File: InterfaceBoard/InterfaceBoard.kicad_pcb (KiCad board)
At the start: 2 copper layers, 100 x 86 mm, 184 parts, among them J1 SWD, J2 USB_B, J3 Keithley_50-Pin_Connector, J4 DB9_Female_MountingHoles, J5 SPI, J6 RS232, J7 UART, J8 I2C, P1 RB1-125BAG1A, Q1 BC848W, Q2 BC848W, Q3 BC848W, Q4 BC856W, SW1 PTS810, SW2 PTS810, U1 W5500, U2 FT231XQ, U3 MAX3232, U4 STM32G0B1RET, U5 AP62250Z6, Y1 25 MHz, Y2 32.768 kHz, Y3 24 MHz

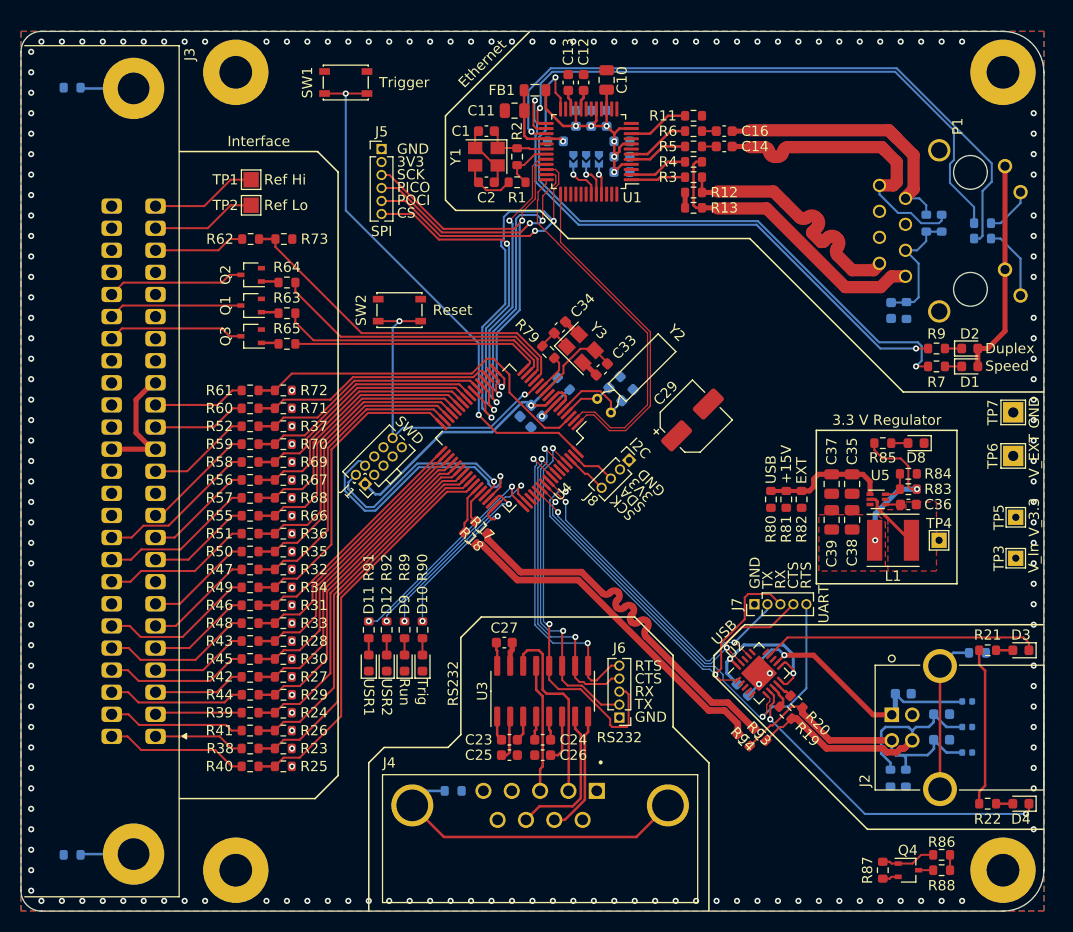
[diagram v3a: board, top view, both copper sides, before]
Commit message: InterfaceBoard: Fully route board.
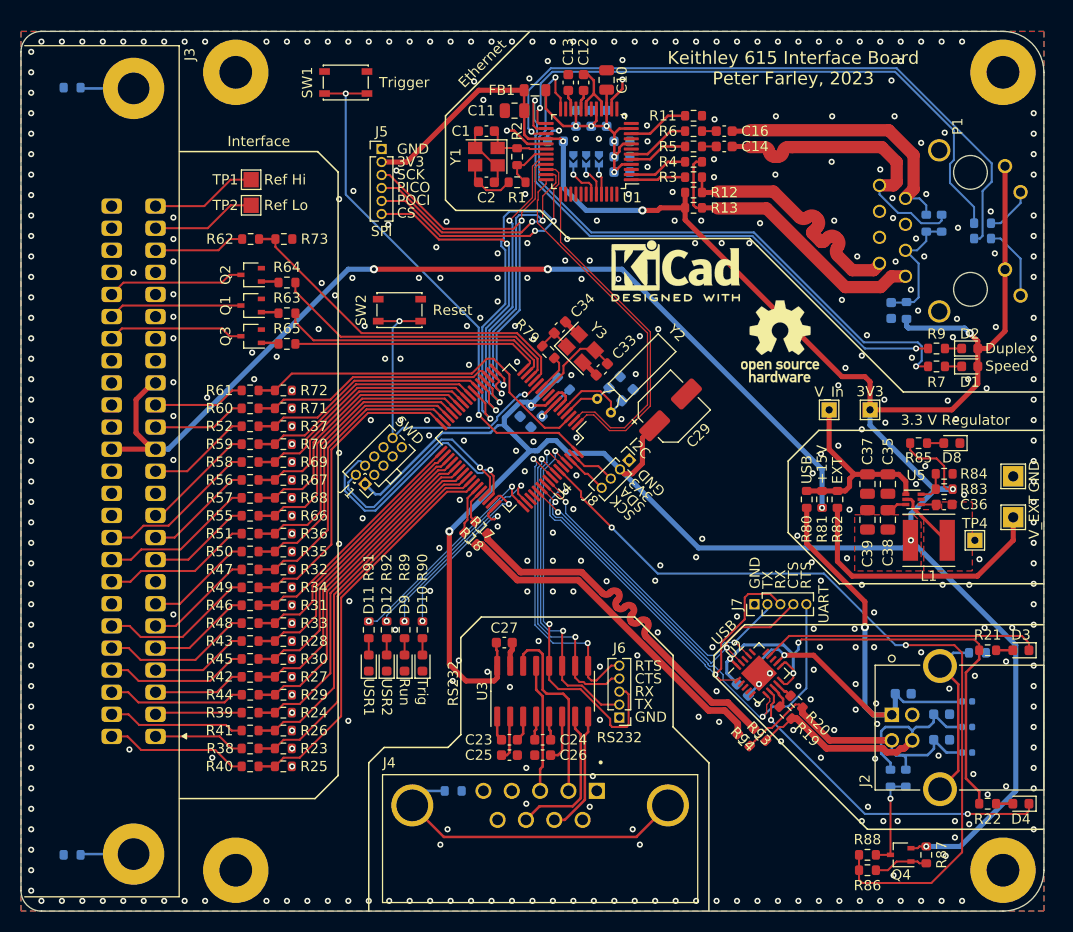
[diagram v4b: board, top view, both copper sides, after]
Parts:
- added REF**: OSHW-Logo_7.5x8mm_SilkScreen, Symbol:OSHW-Logo_7.5x8mm_SilkScreen, F.Cu at (114.2, 59.3)
- added REF**: KiCad-Logo2_5mm_SilkScreen, Symbol:KiCad-Logo2_5mm_SilkScreen, F.Cu at (104.0, 52.4)
- TP5: value V_3.3 -> 3V3
- moved TP3 23.3 mm to (119.0, 66.0), turned to 180 degrees
- moved TP5 17.7 mm to (123.0, 66.0), turned to 180 degrees
- moved R86 7.40 mm to (122.8, 111.0), turned to 0 degrees
- moved R88 7.40 mm to (122.8, 109.5), turned to 180 degrees
- moved TP7 6.25 mm to (137.0, 72.5)
- moved TP6 6.00 mm to (137.0, 76.5)
- moved R87 4.51 mm to (128.5, 109.5), turned to 90 degrees
- moved C35 3.50 mm to (124.8, 73.2)
- moved C36 3.50 mm to (130.2, 75.2)
- moved C37 3.50 mm to (122.8, 73.2)
- moved C38 3.50 mm to (124.8, 76.8)
- moved C39 3.50 mm to (122.8, 76.8)
- moved D8 3.50 mm to (131.0, 69.2)
- moved L1 3.50 mm to (128.8, 78.8)
- moved R80 3.50 mm to (116.8, 74.8)
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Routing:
- net +3V3: track 79.9 -> 300.9 mm, vias 4 -> 8
- net +15V: track 12.7 -> 97.0 mm, vias 0 -> 3
- net /MCU/USB_PULLUP: track 1.50 -> 80.4 mm, vias 0 -> 2
- net /Power Supply/V_EXT: track 0.00 -> 26.7 mm
- net /Power Supply/V_USB: track 27.8 -> 52.5 mm, vias 1 -> 2
- net /USB/FTDI_VCC: track 32.7 -> 53.2 mm, vias 2 -> 3
- net GND: track 15.5 -> 33.2 mm, vias 186 -> 415
- net Net-(R75-Pad2): track 1.43 -> 9.60 mm, vias 0 -> 1
- net /Power Supply/V_IN: track 12.2 -> 19.5 mm
- net /MCU/SWD_SWDIO: track 20.9 -> 22.5 mm
- net Net-(J2-PadSH1): track 15.4 -> 16.9 mm
- net /Ethernet Interface/ETH_PORT_RX+: track 27.5 -> 26.5 mm
- net /MCU/USB_UART_TX: track 34.6 -> 33.8 mm
- net /MCU/RS232_TX: track 33.8 -> 33.0 mm
- net /MCU/RS232_RX: track 39.6 -> 39.0 mm
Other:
- board text added: "Keithley 615 Interface Board Peter Farley, 2023"

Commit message: InterfaceBoard: Geographical reannotation.
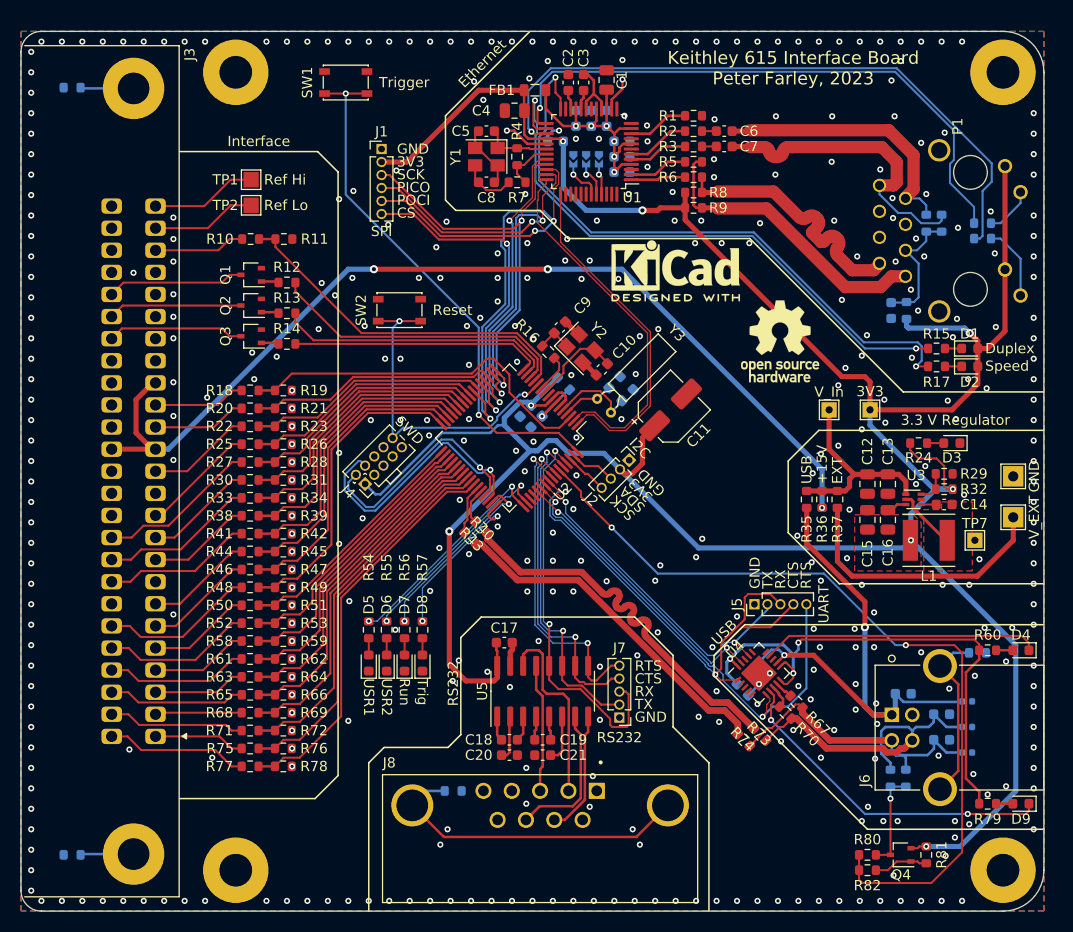
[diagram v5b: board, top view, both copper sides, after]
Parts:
- renumbered C10 to C1, C33 to C10, C29 to C11, C37 to C12, C35 to C13, C36 to C14, C39 to C15, C38 to C16, C27 to C17, C23 to C18, C24 to C19, C13 to C2, C25 to C20, C26 to C21, C6 to C22, C4 to C23, C9 to C24, C3 to C25, C8 to C26, C5 to C27, C7 to C28, C15 to C29, C12 to C3, C31 to C30, C32 to C31, C28 to C32, C30 to C33, C21 to C34, C22 to C35, C20 to C36, C19 to C37, C17 to C38, C18 to C39, C11 to C4, C1 to C5, C16 to C6, C14 to C7, C2 to C8, C34 to C9, D2 to D1, D5 to D10, D7 to D11, D6 to D12, D1 to D2, D8 to D3, D3 to D4, D11 to D5, D12 to D6, D9 to D7, D10 to D8, D4 to D9, H4 to H1, H1 to H4, J5 to J1, J8 to J2, J1 to J4, J7 to J5, J2 to J6, J6 to J7, J4 to J8, Q2 to Q1, Q1 to Q2, R11 to R1, R62 to R10, R73 to R11, R64 to R12, R63 to R13, R65 to R14, R9 to R15, R79 to R16, R7 to R17, R61 to R18, R72 to R19, R6 to R2, R60 to R20, R71 to R21, R52 to R22, R37 to R23, R85 to R24, R59 to R25, R70 to R26, R58 to R27, R69 to R28, R84 to R29, R5 to R3, R56 to R30, R67 to R31, R83 to R32, R57 to R33, R68 to R34, R80 to R35, R81 to R36, R82 to R37, R55 to R38, R66 to R39, R2 to R4, R17 to R40, R51 to R41, R36 to R42, R18 to R43, R50 to R44, R35 to R45, R47 to R46, R32 to R47, R49 to R48, R34 to R49, R4 to R5, R46 to R50, R31 to R51, R48 to R52, R33 to R53, R91 to R54, R92 to R55, R89 to R56, R90 to R57, R43 to R58, R28 to R59, R3 to R6, R21 to R60, R45 to R61, R30 to R62, R42 to R63, R27 to R64, R44 to R65, R29 to R66, R20 to R67, R39 to R68, R24 to R69, R1 to R7, R19 to R70, R41 to R71, R26 to R72, R93 to R73, R94 to R74, R38 to R75, R23 to R76, R40 to R77, R25 to R78, R22 to R79, R12 to R8, R88 to R80, R87 to R81, R86 to R82, R54 to R83, R8 to R84, R16 to R85, R15 to R86, R10 to R87, R14 to R88, R78 to R89, R13 to R9, R74 to R90, R76 to R91, R75 to R92, R77 to R93, R53 to R94, TP5 to TP4, TP7 to TP5, TP4 to TP7, U4 to U2, U5 to U3, U2 to U4, U3 to U5, Y3 to Y2, Y2 to Y3
